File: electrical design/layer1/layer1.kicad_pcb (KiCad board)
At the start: 2 copper layers, 0 parts

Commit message: assign footprints and update layer 1 pcb
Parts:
- added C1: 1μF, Capacitor_SMD:C_0603_1608Metric, F.Cu at (49.0, 110.0)
- added D1: LED, Capacitor_Tantalum_SMD:CP_EIA-3528-12_Kemet-T, B.Cu at (110.0, 48.0)
- added D10: LED, Capacitor_Tantalum_SMD:CP_EIA-3528-12_Kemet-T, B.Cu at (55.1, 120.9)
- added D11: LED, Capacitor_Tantalum_SMD:CP_EIA-3528-12_Kemet-T, B.Cu at (58.3, 131.4)
- added D12: LED, Capacitor_Tantalum_SMD:CP_EIA-3528-12_Kemet-T, B.Cu at (63.4, 141.1)
- added D13: LED, Capacitor_Tantalum_SMD:CP_EIA-3528-12_Kemet-T, B.Cu at (70.4, 149.6)
- added D14: LED, Capacitor_Tantalum_SMD:CP_EIA-3528-12_Kemet-T, B.Cu at (78.9, 156.6)
- added D15: LED, Capacitor_Tantalum_SMD:CP_EIA-3528-12_Kemet-T, B.Cu at (88.6, 161.7)
- added D16: LED, Capacitor_Tantalum_SMD:CP_EIA-3528-12_Kemet-T, B.Cu at (97.9, 170.8)
- added D17: LED, Capacitor_Tantalum_SMD:CP_EIA-3528-12_Kemet-T, B.Cu at (110.0, 172.0)
- added D18: LED, Capacitor_Tantalum_SMD:CP_EIA-3528-12_Kemet-T, B.Cu at (122.1, 170.8)
- added D19: LED, Capacitor_Tantalum_SMD:CP_EIA-3528-12_Kemet-T, B.Cu at (131.4, 161.7)
- added D2: LED, Capacitor_Tantalum_SMD:CP_EIA-3528-12_Kemet-T, B.Cu at (97.9, 49.2)
- added D20: LED, Capacitor_Tantalum_SMD:CP_EIA-3528-12_Kemet-T, B.Cu at (141.1, 156.6)
- added D21: LED, Capacitor_Tantalum_SMD:CP_EIA-3528-12_Kemet-T, B.Cu at (149.6, 149.6)
- added D22: LED, Capacitor_Tantalum_SMD:CP_EIA-3528-12_Kemet-T, B.Cu at (156.6, 141.1)
- added D23: LED, Capacitor_Tantalum_SMD:CP_EIA-3528-12_Kemet-T, B.Cu at (161.7, 131.4)
- added D24: LED, Capacitor_Tantalum_SMD:CP_EIA-3528-12_Kemet-T, B.Cu at (164.9, 120.9)
- added D25: LED, Capacitor_Tantalum_SMD:CP_EIA-3528-12_Kemet-T, B.Cu at (166.0, 110.0)
- added D26: LED, Capacitor_Tantalum_SMD:CP_EIA-3528-12_Kemet-T, B.Cu at (164.9, 99.1)
- added D27: LED, Capacitor_Tantalum_SMD:CP_EIA-3528-12_Kemet-T, B.Cu at (161.7, 88.6)
- added D28: LED, Capacitor_Tantalum_SMD:CP_EIA-3528-12_Kemet-T, B.Cu at (156.6, 78.9)
- added D29: LED, Capacitor_Tantalum_SMD:CP_EIA-3528-12_Kemet-T, B.Cu at (149.6, 70.4)
- added D3: LED, Capacitor_Tantalum_SMD:CP_EIA-3528-12_Kemet-T, B.Cu at (88.6, 58.3)
- added D30: LED, Capacitor_Tantalum_SMD:CP_EIA-3528-12_Kemet-T, B.Cu at (141.1, 63.4)
- added D31: LED, Capacitor_Tantalum_SMD:CP_EIA-3528-12_Kemet-T, B.Cu at (131.4, 58.3)
- added D32: LED, Capacitor_Tantalum_SMD:CP_EIA-3528-12_Kemet-T, B.Cu at (122.1, 49.2)
- added D4: LED, Capacitor_Tantalum_SMD:CP_EIA-3528-12_Kemet-T, B.Cu at (78.9, 63.4)
- added D5: LED, Capacitor_Tantalum_SMD:CP_EIA-3528-12_Kemet-T, B.Cu at (70.4, 70.4)
- added D6: LED, Capacitor_Tantalum_SMD:CP_EIA-3528-12_Kemet-T, B.Cu at (63.4, 78.9)
- added D7: LED, Capacitor_Tantalum_SMD:CP_EIA-3528-12_Kemet-T, B.Cu at (58.3, 88.6)
- added D8: LED, Capacitor_Tantalum_SMD:CP_EIA-3528-12_Kemet-T, B.Cu at (55.1, 99.1)
- added D9: LED, Capacitor_Tantalum_SMD:CP_EIA-3528-12_Kemet-T, B.Cu at (54.0, 110.0)
- added J2: Conn_01x06_Female, Connector_JST:JST_SH_BM06B-SRSS-TB_1x06-1MP_P1.00mm_Vertical, F.Cu at (139.0, 100.0)
- added R1: ALS-PT19-315C, Diode_SMD:D_0603_1608Metric, B.Cu at (103.9, 48.3)
- added R10: ALS-PT19-315C, Diode_SMD:D_0603_1608Metric, B.Cu at (56.4, 126.3)
- added R11: ALS-PT19-315C, Diode_SMD:D_0603_1608Metric, B.Cu at (60.6, 136.4)
- added R12: ALS-PT19-315C, Diode_SMD:D_0603_1608Metric, B.Cu at (66.7, 145.5)
- added R13: ALS-PT19-315C, Diode_SMD:D_0603_1608Metric, B.Cu at (74.5, 153.3)
- added R14: ALS-PT19-315C, Diode_SMD:D_0603_1608Metric, B.Cu at (83.6, 159.4)
- added R15: ALS-PT19-315C, Diode_SMD:D_0603_1608Metric, B.Cu at (93.7, 163.6)
- added R16: ALS-PT19-315C, Diode_SMD:D_0603_1608Metric, B.Cu at (103.9, 171.7)
- added R17: ALS-PT19-315C, Diode_SMD:D_0603_1608Metric, B.Cu at (116.1, 171.7)
- added R18: ALS-PT19-315C, Diode_SMD:D_0603_1608Metric, B.Cu at (126.3, 163.6)
- added R19: ALS-PT19-315C, Diode_SMD:D_0603_1608Metric, B.Cu at (136.4, 159.4)
- added R2: ALS-PT19-315C, Diode_SMD:D_0603_1608Metric, B.Cu at (93.7, 56.4)
- added R20: ALS-PT19-315C, Diode_SMD:D_0603_1608Metric, B.Cu at (145.5, 153.3)
- added R21: ALS-PT19-315C, Diode_SMD:D_0603_1608Metric, B.Cu at (153.3, 145.5)
- added R22: ALS-PT19-315C, Diode_SMD:D_0603_1608Metric, B.Cu at (159.4, 136.4)
- added R23: ALS-PT19-315C, Diode_SMD:D_0603_1608Metric, B.Cu at (163.6, 126.3)
- added R24: ALS-PT19-315C, Diode_SMD:D_0603_1608Metric, B.Cu at (165.7, 115.5)
- added R25: ALS-PT19-315C, Diode_SMD:D_0603_1608Metric, B.Cu at (165.7, 104.5)
- added R26: ALS-PT19-315C, Diode_SMD:D_0603_1608Metric, B.Cu at (163.6, 93.7)
- added R27: ALS-PT19-315C, Diode_SMD:D_0603_1608Metric, B.Cu at (159.4, 83.6)
- added R28: ALS-PT19-315C, Diode_SMD:D_0603_1608Metric, B.Cu at (153.3, 74.5)
- added R29: ALS-PT19-315C, Diode_SMD:D_0603_1608Metric, B.Cu at (145.5, 66.7)
- added R3: ALS-PT19-315C, Diode_SMD:D_0603_1608Metric, B.Cu at (83.6, 60.6)
- added R30: ALS-PT19-315C, Diode_SMD:D_0603_1608Metric, B.Cu at (136.4, 60.6)
- added R31: ALS-PT19-315C, Diode_SMD:D_0603_1608Metric, B.Cu at (126.3, 56.4)
- added R32: ALS-PT19-315C, Diode_SMD:D_0603_1608Metric, B.Cu at (116.1, 48.3)
- added R4: ALS-PT19-315C, Diode_SMD:D_0603_1608Metric, B.Cu at (74.5, 66.7)
- added R5: ALS-PT19-315C, Diode_SMD:D_0603_1608Metric, B.Cu at (66.7, 74.5)
- added R6: ALS-PT19-315C, Diode_SMD:D_0603_1608Metric, B.Cu at (60.6, 83.6)
- added R7: ALS-PT19-315C, Diode_SMD:D_0603_1608Metric, B.Cu at (56.4, 93.7)
- added R8: ALS-PT19-315C, Diode_SMD:D_0603_1608Metric, B.Cu at (54.3, 104.5)
- added R9: ALS-PT19-315C, Diode_SMD:D_0603_1608Metric, B.Cu at (54.3, 115.5)
- added U1: STM32F103C8T6, Package_QFP:LQFP-48_7x7mm_P0.5mm, F.Cu at (110.0, 110.0)
- added U2: CD74HC4067SM, Package_SO:SSOP-24_5.3x8.2mm_P0.65mm, B.Cu at (110.0, 94.0)
- added U3: CD74HC4067SM, Package_SO:SSOP-24_5.3x8.2mm_P0.65mm, B.Cu at (110.0, 126.0)
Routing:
- net VCCQ: track 0.00 -> 373.1 mm, vias 0 -> 8
- net Net-(R16-Pad2): track 0.00 -> 87.2 mm
- net Net-(R32-Pad2): track 0.00 -> 86.5 mm
- net Net-(R31-Pad2): track 0.00 -> 72.3 mm
- net Net-(R15-Pad2): track 0.00 -> 72.3 mm
- net Net-(R14-Pad2): track 0.00 -> 72.0 mm
- net Net-(R30-Pad2): track 0.00 -> 72.0 mm
- net Net-(R13-Pad2): track 0.00 -> 69.5 mm
- net Net-(R29-Pad2): track 0.00 -> 69.5 mm
- net Net-(R28-Pad2): track 0.00 -> 64.7 mm
- net Net-(R12-Pad2): track 0.00 -> 64.7 mm
- net Net-(R27-Pad2): track 0.00 -> 63.6 mm
- net Net-(R11-Pad2): track 0.00 -> 63.6 mm
- net Net-(R26-Pad2): track 0.00 -> 63.0 mm
- net Net-(R10-Pad2): track 0.00 -> 63.0 mm
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- added copper zone on F.Cu, net GND
- added copper zone on B.Cu, net Net-(C1-Pad1)
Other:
- board outline added: 178 x 158.1 mm

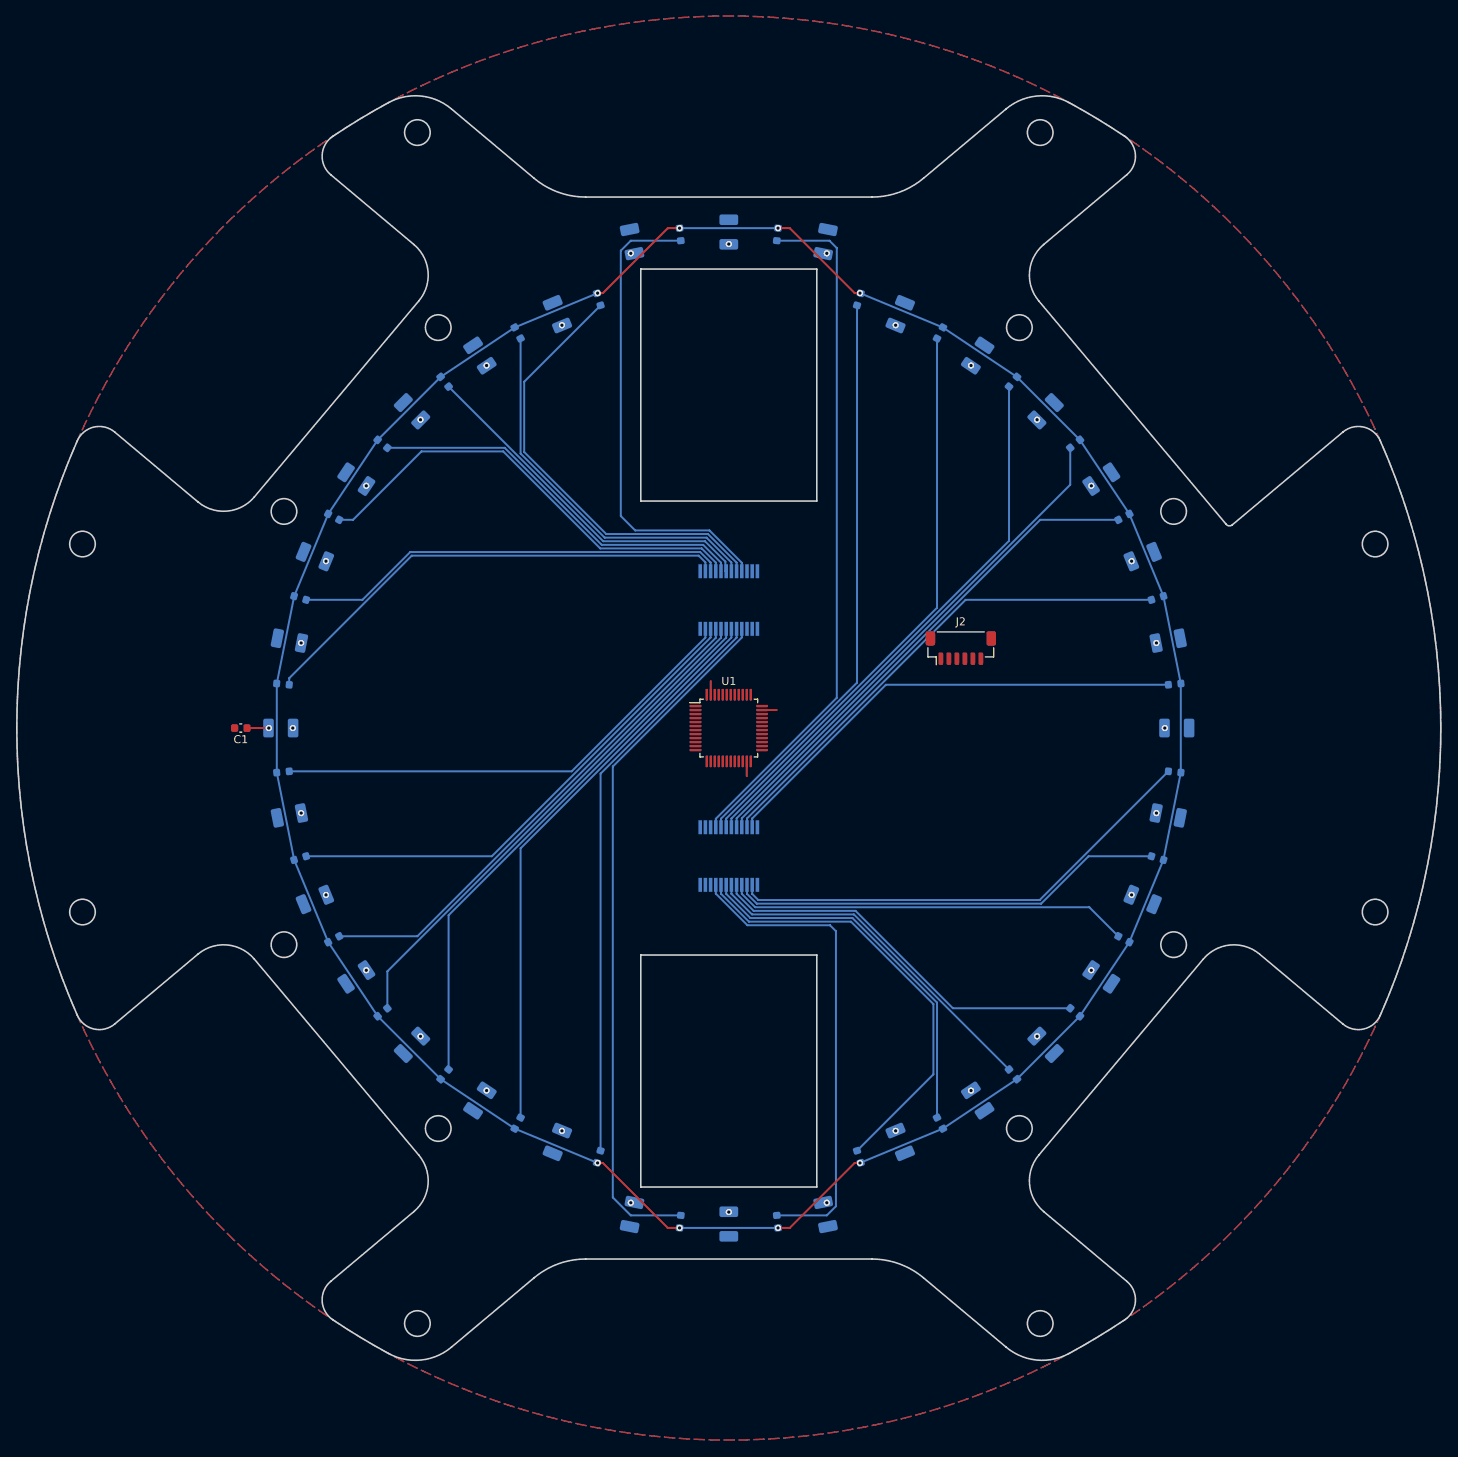
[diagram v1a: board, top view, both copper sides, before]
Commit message: add solenoid circuit and custom board rules
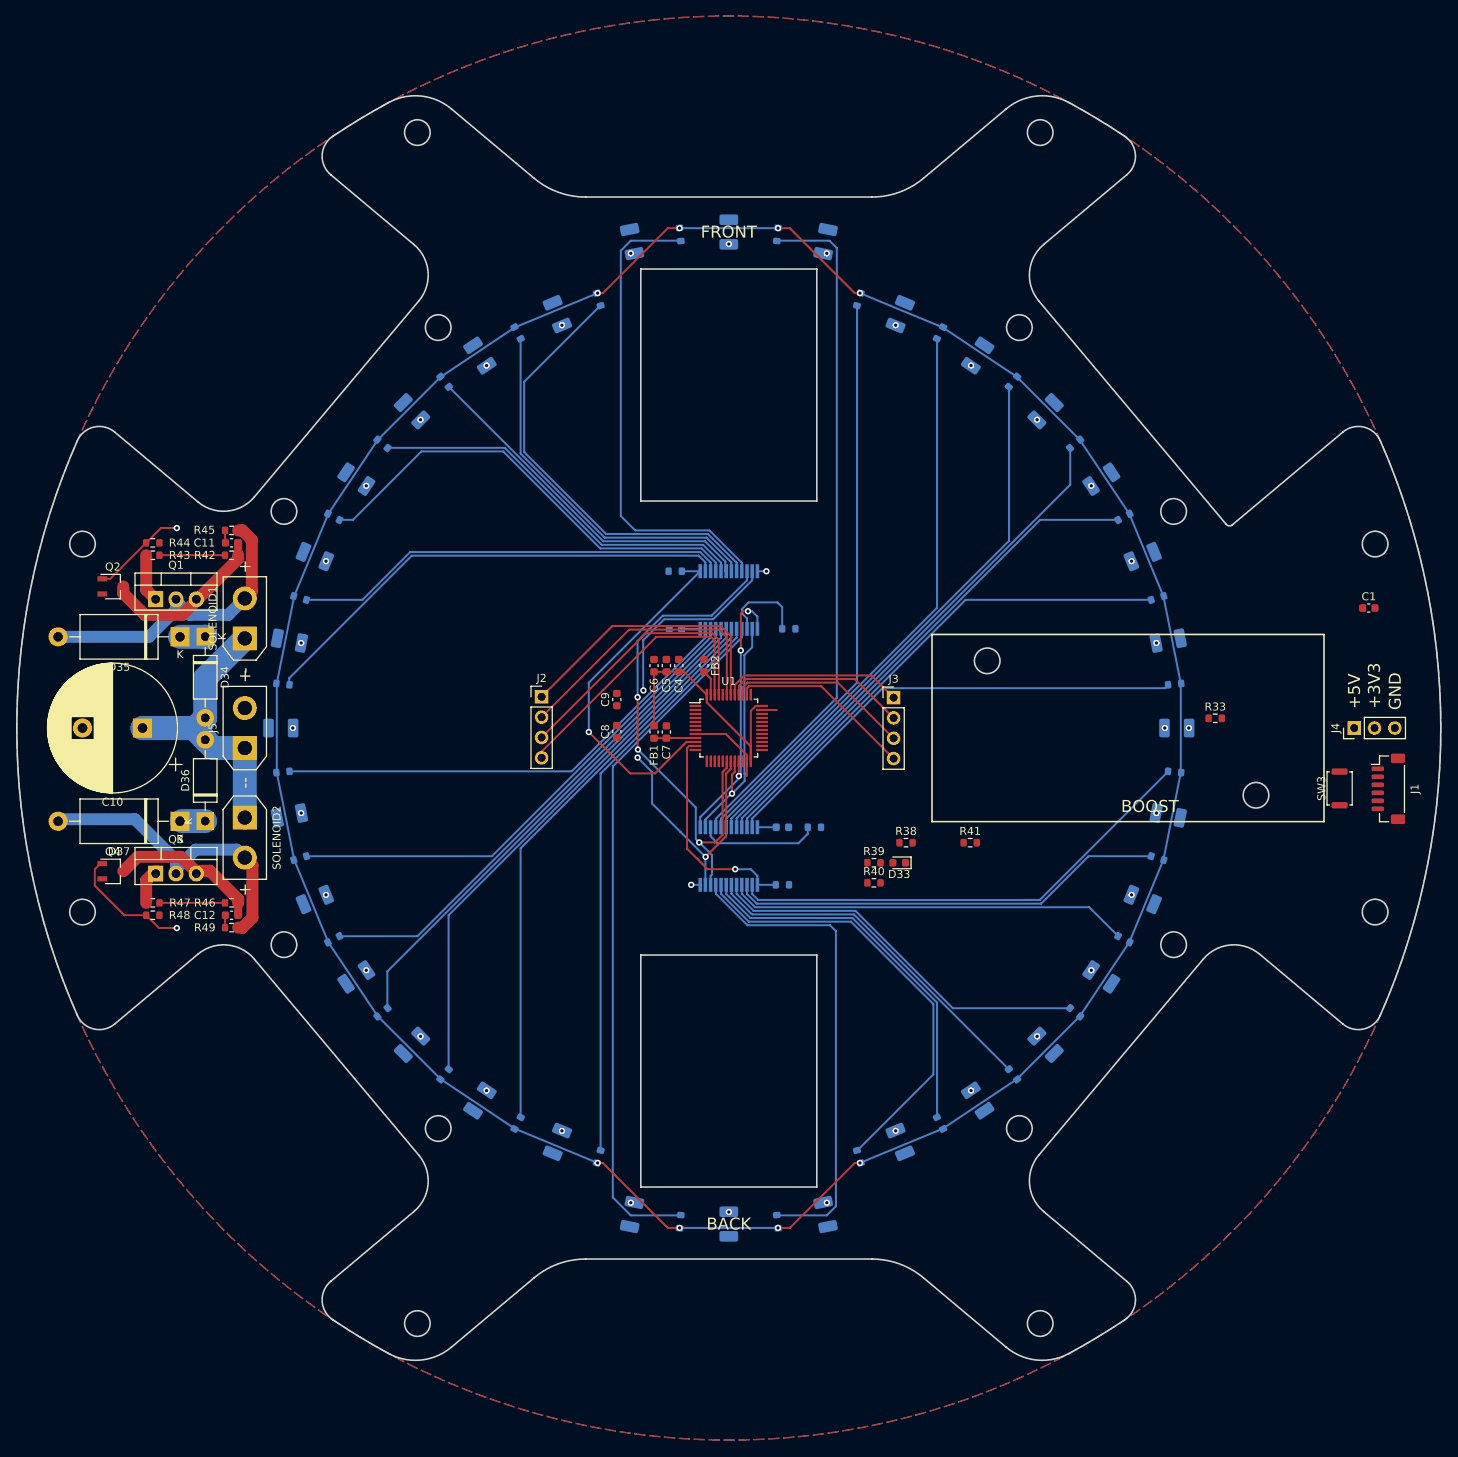
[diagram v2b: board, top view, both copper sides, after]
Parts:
- added C10: 1000µF/63V, Capacitor_THT:CP_Radial_D16.0mm_P7.50mm, F.Cu at (36.7, 110.0)
- added C11: 1500pF, Capacitor_SMD:C_0603_1608Metric, F.Cu at (47.9, 86.8)
- added C12: 1500pF, Capacitor_SMD:C_0603_1608Metric, F.Cu at (47.9, 133.4)
- added C2: 0.1μF, Capacitor_SMD:C_0603_1608Metric, B.Cu at (116.7, 122.4)
- added C3: 0.1μF, Capacitor_SMD:C_0603_1608Metric, B.Cu at (103.3, 97.6)
- added C4: 1μF, Capacitor_SMD:C_0603_1608Metric, F.Cu at (103.8, 102.2)
- added C5: 1μF, Capacitor_SMD:C_0603_1608Metric, F.Cu at (102.2, 102.2)
- added C6: 1μF, Capacitor_SMD:C_0603_1608Metric, F.Cu at (100.7, 102.2)
- added C7: 1μF, Capacitor_SMD:C_0603_1608Metric, F.Cu at (102.2, 110.5)
- added C8: 1pF, Capacitor_SMD:C_0603_1608Metric, F.Cu at (96.0, 110.5)
- added C9: 1pF, Capacitor_SMD:C_0603_1608Metric, F.Cu at (96.0, 106.4)
- added D33: BLUE, Diode_SMD:D_0603_1608Metric, F.Cu at (131.3, 126.8)
- added D34: 1N4728, Diode_THT:D_DO-41_SOD81_P10.16mm_Horizontal, F.Cu at (44.5, 98.6)
- added D35: 1N5401, Diode_THT:D_DO-27_P15.24mm_Horizontal, F.Cu at (41.4, 98.6)
- added D36: 1N4728, Diode_THT:D_DO-41_SOD81_P10.16mm_Horizontal, F.Cu at (44.5, 121.6)
- added D37: 1N5401, Diode_THT:D_DO-27_P15.24mm_Horizontal, F.Cu at (41.4, 121.7)
- added FB1: 30Ω/1.8A, Capacitor_SMD:C_0603_1608Metric, F.Cu at (100.7, 110.5)
- added FB2: 30Ω/1.8A, Capacitor_SMD:C_0603_1608Metric, F.Cu at (106.9, 102.2)
- added J2: Conn_01x04_Male, Connector_PinHeader_2.54mm:PinHeader_1x04_P2.54mm_Vertical, F.Cu at (86.6, 106.1)
- added J3: Conn_01x04_Male, Connector_PinHeader_2.54mm:PinHeader_1x04_P2.54mm_Vertical, F.Cu at (130.6, 106.2)
- added J4: Conn_01x03_Female, Connector_PinHeader_2.54mm:PinHeader_1x03_P2.54mm_Vertical, F.Cu at (188.2, 110.0)
- added J5: Conn_01x02_Female, Connector_AMASS:AMASS_XT30UPB-F_1x02_P5.0mm_Vertical, F.Cu at (49.5, 112.5)
- added Q1: MOSFET-NCH-FQP30N06L, Package_TO_SOT_THT:TO-220-3_Vertical, F.Cu at (38.4, 93.9)
- added Q2: MOSFET-NCH-AO3404A, Package_TO_SOT_SMD:TSOT-23, F.Cu at (33.0, 92.3)
- added Q3: MOSFET-NCH-FQP30N06L, Package_TO_SOT_THT:TO-220-3_Vertical, F.Cu at (38.4, 128.2)
- added Q4: MOSFET-NCH-AO3404A, Package_TO_SOT_SMD:TSOT-23, F.Cu at (33.0, 127.9)
- added R33: 0.39, Resistor_SMD:R_0603_1608Metric, F.Cu at (170.8, 108.8)
- added R34: 3k, Resistor_SMD:R_0603_1608Metric, B.Cu at (103.3, 90.4)
- added R35: 10k, Resistor_SMD:R_0603_1608Metric, B.Cu at (117.5, 97.6)
- added R36: 3k, Resistor_SMD:R_0603_1608Metric, B.Cu at (116.7, 129.6)
- added R37: 10k, Resistor_SMD:R_0603_1608Metric, B.Cu at (120.7, 122.4)
- added R38: 10k, Resistor_SMD:R_0603_1608Metric, F.Cu at (132.2, 124.3)
- added R39: 1k, Resistor_SMD:R_0603_1608Metric, F.Cu at (128.1, 126.8)
- added R40: 1k, Resistor_SMD:R_0603_1608Metric, F.Cu at (128.1, 129.3)
- added R41: 10k, Resistor_SMD:R_0603_1608Metric, F.Cu at (140.2, 124.3)
- added R42: 10k, Resistor_SMD:R_0603_1608Metric, F.Cu at (47.9, 88.4)
- added R43: 1k, Resistor_SMD:R_0603_1608Metric, F.Cu at (38.0, 88.4)
- added R44: 10k, Resistor_SMD:R_0603_1608Metric, F.Cu at (38.0, 86.8)
- added R45: 20, Resistor_SMD:R_0603_1608Metric, F.Cu at (47.9, 85.3)
- added R46: 10k, Resistor_SMD:R_0603_1608Metric, F.Cu at (47.9, 131.8)
- added R47: 1k, Resistor_SMD:R_0603_1608Metric, F.Cu at (38.0, 131.8)
- added R48: 10k, Resistor_SMD:R_0603_1608Metric, F.Cu at (38.0, 133.4)
- added R49: 20, Resistor_SMD:R_0603_1608Metric, F.Cu at (47.9, 134.9)
- added SOLENOID1: Conn_01x02_Female, Connector_AMASS:AMASS_XT30UPB-F_1x02_P5.0mm_Vertical, F.Cu at (49.5, 98.8)
- added SOLENOID2: Conn_01x02_Female, Connector_AMASS:AMASS_XT30UPB-F_1x02_P5.0mm_Vertical, F.Cu at (49.5, 121.2)
- added SW3: SW_Push, Button_Switch_SMD:SW_Push_SPST_NO_Alps_SKRK, F.Cu at (186.3, 117.5)
- R1, R10, R11, R12, R13, R14, R15, R16, R17, R18, R19, R2, R20, R21, R22, R23, R24, R25, R26, R27, R28, R29, R3, R30, R31, R32, R4, R5, R6, R7, R8, R9: footprint Diode_SMD:D_0603_1608Metric -> Resistor_SMD:R_0603_1608Metric
- moved C1 141.8 mm to (190.0, 95.0), turned to 0 degrees
- moved J1 56.3 mm to (192.4, 117.6), turned to -90 degrees
- renumbered J2 to J1
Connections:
- U1 pad 17: unconnected-(U1-Pad17) -> /SOLENOID1ON
- U1 pad 29: unconnected-(U1-Pad29) -> /SOLENOID2ON
- U1 pad 38: /M1EA -> /M4EB
- U1 pad 39: /M1EB -> /M4EA
- U1 pad 40: /M2EA -> /M2EB
- U1 pad 41: /M2EB -> /M2EA
- U1 pad 42: /M3EA -> /M1EA
- U1 pad 43: /M3EB -> /M1EB
- U1 pad 45: /M4EA -> /M3EA
- U1 pad 46: /M4EB -> /M3EB
- U1 pad 47: GND -> GNDA
- U1 pad 8: GNDA -> GND
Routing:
- net /S0: track 0.00 -> 65.1 mm, vias 0 -> 3
- net /S1: track 0.00 -> 57.0 mm, vias 0 -> 3
- net /MUX1OUT: track 0.00 -> 45.3 mm, vias 0 -> 1
- net /SOLENOIDPOWER: track 0.00 -> 42.9 mm
- net Net-(D37-Pad2): track 0.00 -> 38.6 mm
- net Net-(SOLENOID1-Pad2): track 0.00 -> 37.7 mm
- net /M3EB: track 0.00 -> 35.3 mm
- net /M1EB: track 0.00 -> 35.3 mm
- net /M1EA: track 0.00 -> 35.2 mm
- net /M3EA: track 0.00 -> 34.8 mm
- net /S3: track 0.00 -> 34.6 mm, vias 0 -> 3
- net /MCU3V3: track 0.00 -> 33.1 mm
- net /S2: track 0.00 -> 31.5 mm, vias 0 -> 1
- net /MUX2OUT: track 0.00 -> 27.4 mm, vias 0 -> 1
- net /M4EB: track 0.00 -> 23.0 mm
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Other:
- outline, holes or cut-outs redrawn
- board text added: "+3V3"
- board text added: "+5V"
- board text added: "BACK"
- board text added: "BOOST"
- board text added: "FRONT"
- board text added: "GND"
